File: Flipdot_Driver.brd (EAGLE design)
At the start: 160 x 100 mm, 27 parts

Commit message: Finished driver board design
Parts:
- added U$6: 3_PIN, Flipdot:3_PIN
- moved U$5 197.9 mm to (114.9, 74.2)
- moved U$4 155.3 mm to (126.9, 26.2)
- moved U$11 125.5 mm to (-22.1, 78.2), turned to 270 degrees
- moved U$10 116.5 mm to (-10.1, 76.2), turned to 270 degrees
- moved U$3 52.2 mm to (-24.0, 37.2), turned to 270 degrees
- moved SUBSEG 19.1 mm to (-16.5, 30.8)
- moved U$2 11.5 mm to (-20.7, -0.60), turned to 90 degrees
- moved COL_D_HL 0.58 mm to (88.3, 78.0)
- moved ROW_L 0.22 mm to (113.0, 53.7)
- moved SINK_R 0.22 mm to (101.9, 48.5)
- moved SOURCE_D 0.22 mm to (84.4, 64.1)
- moved COL_C_H 0.22 mm to (16.8, 75.9)
- moved COL_C_L 0.22 mm to (39.8, 75.9)
- moved SINK_C 0.22 mm to (37.3, 64.8)
- moved U$1 0.22 mm to (60.4, 40.8)
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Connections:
- net A: now also U$6.P$1
- net B: now also U$6.P$2
- net C: now also U$6.P$3
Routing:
- net N$13: track 0.00 -> 334.1 mm, vias 0 -> 2
- net 5V: track 174.3 -> 456.0 mm, vias 2 -> 12
- net GND: track 458.8 -> 685.9 mm, vias 2 -> 6
- net 10V: track 114.8 -> 313.9 mm, vias 2 -> 9
- net N$7: track 0.00 -> 159.8 mm, vias 0 -> 4
- net N$9: track 0.00 -> 156.1 mm, vias 0 -> 2
- net N$12: track 0.00 -> 115.1 mm, vias 0 -> 2
- net N$10: track 0.00 -> 108.1 mm, vias 0 -> 2
- net N$11: track 0.00 -> 87.8 mm
- net N$8: track 0.00 -> 85.2 mm, vias 0 -> 4
- net SEG_1: track 0.00 -> 71.4 mm, vias 0 -> 1
- net B: track 195.4 -> 251.5 mm, vias 3 -> 9
- net A: track 181.7 -> 229.7 mm, vias 7 -> 10
- net C: track 196.2 -> 240.8 mm, vias 4 -> 5
- net N$80: track 0.00 -> 14.9 mm
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
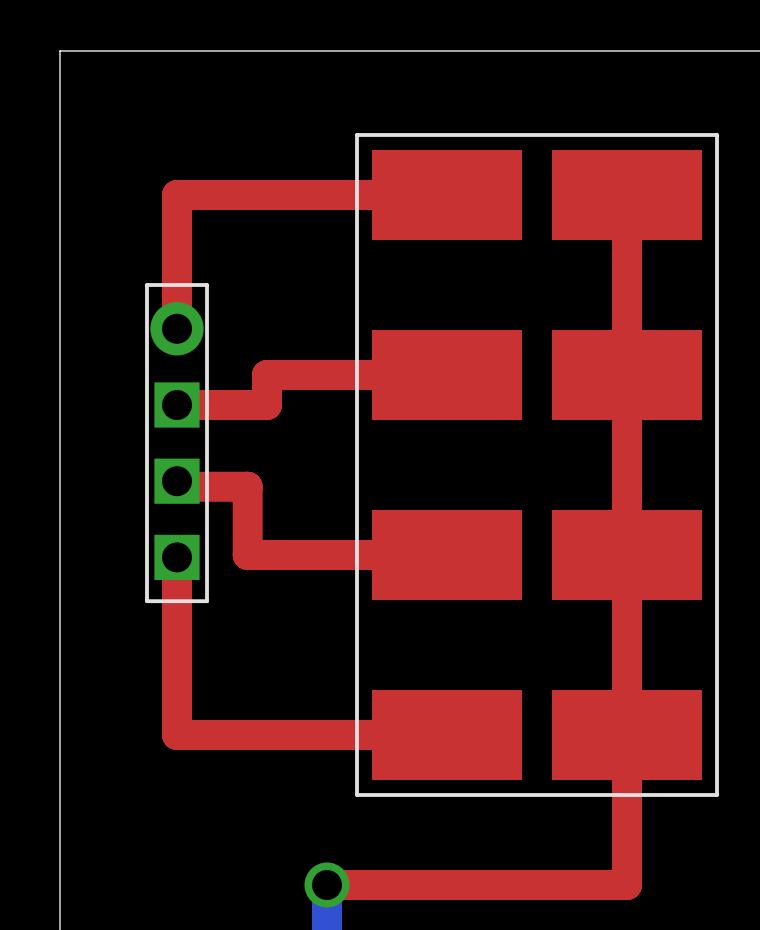
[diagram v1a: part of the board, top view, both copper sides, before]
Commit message: Fixed layering issue, finished printing stencil
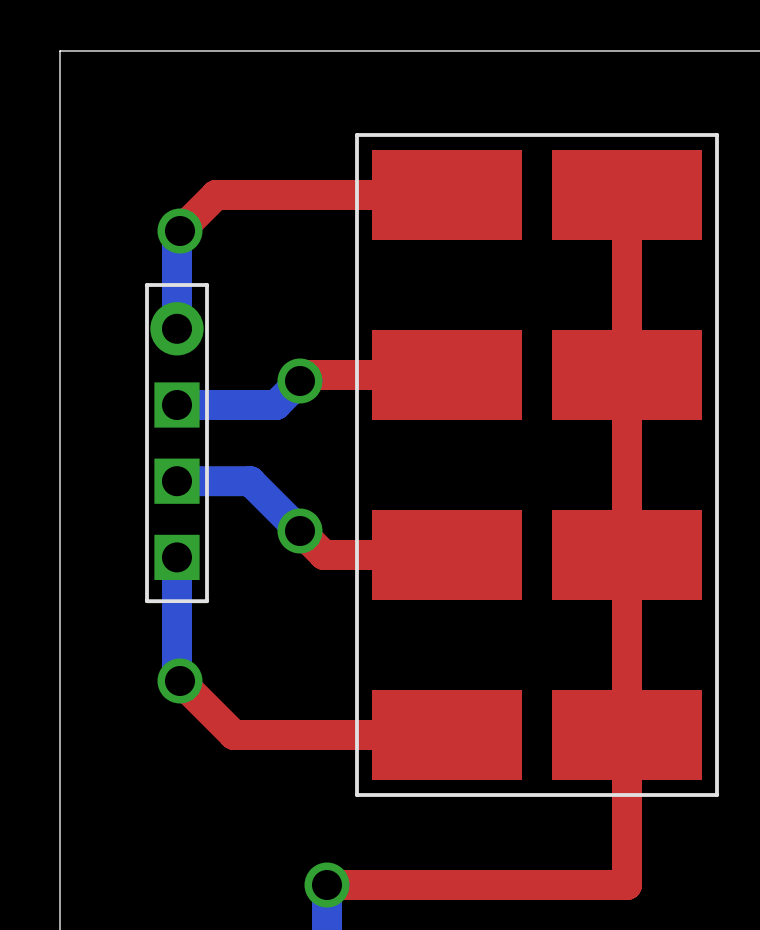
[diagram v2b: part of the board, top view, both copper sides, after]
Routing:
- net N$3: track 11.5 -> 10.0 mm, vias 0 -> 1
- net N$80: track 14.9 -> 13.8 mm, vias 0 -> 1
- net N$1: track 13.5 -> 12.7 mm, vias 0 -> 1
- net N$2: track 10.0 -> 9.41 mm, vias 0 -> 1
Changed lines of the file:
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@@
 <wire x1="134" y1="90" x2="-26" y2="90" width="0" layer="20"/>
 <wire x1="-26" y1="90" x2="-26" y2="-10" width="0" layer="20"/>
-<dimension x1="134" y1="-10" x2="134" y2="90" x3="138" y3="40" textsize="1.778" layer="20"/>
-<dimension x1="134" y1="90" x2="-26" y2="90" x3="54" y3="93" textsize="1.778" layer="20"/>
 </plain>
 <attributes>
@@
 <contactref element="U$11" pad="P$1"/>
 <contactref element="U$10" pad="S1"/>
-<wire x1="-22.1" y1="80.74" x2="-22.1" y2="85.2" width="1" layer="1"/>
-<wire x1="-22.1" y1="85.2" x2="-13.1" y2="85.2" width="1" layer="1"/>
+<wire x1="-13.1" y1="85.2" x2="-20.8" y2="85.2" width="1" layer="1"/>
+<wire x1="-20.8" y1="85.2" x2="-22" y2="84" width="1" layer="1"/>
+<via x="-22" y="84" extent="1-16" drill="1"/>
+<wire x1="-22" y1="84" x2="-22.1" y2="83.9" width="1" layer="16"/>
+<wire x1="-22.1" y1="83.9" x2="-22.1" y2="80.74" width="1" layer="16"/>
 </signal>
 <signal name="N$2">
 <contactref element="U$11" pad="P$2"/>
 <contactref element="U$10" pad="S2"/>
-<wire x1="-22.1" y1="78.2" x2="-19.1" y2="78.2" width="1" layer="1"/>
-<wire x1="-19.1" y1="78.2" x2="-19.1" y2="79.2" width="1" layer="1"/>
-<wire x1="-19.1" y1="79.2" x2="-13.1" y2="79.2" width="1" layer="1"/>
+<wire x1="-13.1" y1="79.2" x2="-17.8" y2="79.2" width="1" layer="1"/>
+<wire x1="-17.8" y1="79.2" x2="-18" y2="79" width="1" layer="1"/>
+<via x="-18" y="79" extent="1-16" drill="1"/>
+<wire x1="-18" y1="79" x2="-18.8" y2="78.2" width="1" layer="16"/>
+<wire x1="-18.8" y1="78.2" x2="-22.1" y2="78.2" width="1" layer="16"/>
 </signal>
 <signal name="N$3">
 <contactref element="U$11" pad="P$3"/>
 <contactref element="U$10" pad="S3"/>
-<wire x1="-22.1" y1="75.66" x2="-22.1" y2="75.4756" width="1" layer="1"/>
-<wire x1="-22.1" y1="75.4756" x2="-19.7444" y2="75.4756" width="1" layer="1"/>
-<wire x1="-19.7444" y1="75.4756" x2="-19.7444" y2="73.2" width="1" layer="1"/>
-<wire x1="-19.7444" y1="73.2" x2="-13.1" y2="73.2" width="1" layer="1"/>
+<wire x1="-13.1" y1="73.2" x2="-17.2" y2="73.2" width="1" layer="1"/>
+<wire x1="-17.2" y1="73.2" x2="-18" y2="74" width="1" layer="1"/>
+<via x="-18" y="74" extent="1-16" drill="1"/>
+<wire x1="-18" y1="74" x2="-19.66" y2="75.66" width="1" layer="16"/>
+<wire x1="-19.66" y1="75.66" x2="-22.1" y2="75.66" width="1" layer="16"/>
 </signal>
 <signal name="N$80">
 <contactref element="U$11" pad="P$4"/>
 <contactref element="U$10" pad="S4"/>
-<wire x1="-22.1" y1="73.12" x2="-22.1" y2="67.2" width="1" layer="1"/>
-<wire x1="-22.1" y1="67.2" x2="-13.1" y2="67.2" width="1" layer="1"/>
+<wire x1="-13.1" y1="67.2" x2="-20.2" y2="67.2" width="1" layer="1"/>
+<wire x1="-20.2" y1="67.2" x2="-22" y2="69" width="1" layer="1"/>
+<via x="-22" y="69" extent="1-16" drill="1"/>
+<wire x1="-22" y1="69" x2="-22.1" y2="69.1" width="1" layer="16"/>
+<wire x1="-22.1" y1="69.1" x2="-22.1" y2="73.12" width="1" layer="16"/>
 </signal>
 <signal name="N$4">

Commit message: Finished, sent for production review
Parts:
- removed U$6: 3_PIN, Flipdot:3_PIN
- moved U$2 38.0 mm to (15.5, 10.8)
- moved U$3 33.1 mm to (6.62, 49.7), turned to 0 degrees
- moved U$11 31.2 mm to (5.97, 64.6)
- moved U$10 27.8 mm to (14.7, 63.5)
- moved COL_C_L 26.1 mm to (63.3, 64.5)
- moved SINK_C 26.1 mm to (60.8, 53.3)
- moved SOURCE_C 26.1 mm to (36.5, 53.3)
- moved COL_C_H 26.1 mm to (40.3, 64.5)
- moved SOURCE_D 25.8 mm to (107.9, 53.5)
- moved SINK_D 25.8 mm to (83.7, 53.4)
- moved COL_A_L 25.1 mm to (77.9, 10.5)
- moved SINK_A 25.1 mm to (80.3, 21.9)
- moved SOURCE_A 25.1 mm to (105.2, 21.7)
- moved COL_A_H 25.1 mm to (101.3, 10.4)
- moved COL_B_H 23.6 mm to (31.1, 10.5)
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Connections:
- net A: no longer U$6.P$1
- net B: no longer U$6.P$2
- net C: no longer U$6.P$3
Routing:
- net N$13: track 334.1 -> 120.7 mm, vias 2 -> 1
- net GND: track 685.9 -> 519.3 mm, vias 6 -> 3
- net 5V: track 456.0 -> 305.1 mm, vias 12 -> 3
- net 10V: track 313.9 -> 229.4 mm, vias 9 -> 2
- net N$7: track 159.8 -> 97.6 mm, vias 4 -> 2
- net N$8: track 85.2 -> 48.0 mm, vias 4 -> 2
- net N$10: track 108.1 -> 72.0 mm
- net N$9: track 156.1 -> 122.1 mm, vias 2 -> 0
- net C1: track 61.2 -> 37.0 mm
- net N$12: track 115.1 -> 91.5 mm
- net SEG_1: track 71.4 -> 48.4 mm
- net N$11: track 87.8 -> 65.4 mm
- net C3: track 59.1 -> 36.7 mm, vias 2 -> 1
- net C2: track 63.1 -> 41.5 mm
- net C20: track 68.1 -> 46.9 mm
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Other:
- board size 160 x 100 mm -> 146 x 75.9 mm
- board text added: "GND 5V 10V"
- board text added: "MCU 2 3 4"
- board text added: "MCU 5 6 7"
- board text added: "MCU 8 9 10"
- board text added: "Seg. Sel."
- board text added: "The cake is a lie."

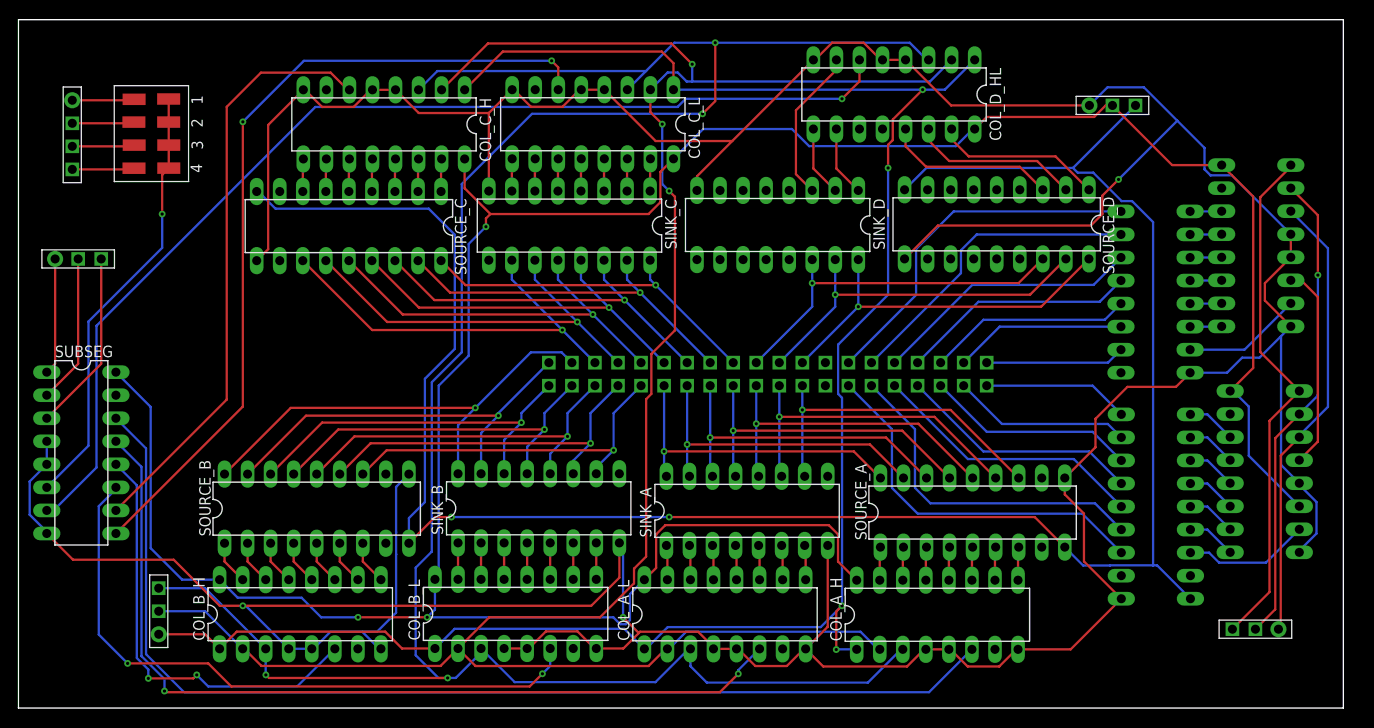
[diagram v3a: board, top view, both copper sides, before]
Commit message: Fixed missing RE connector
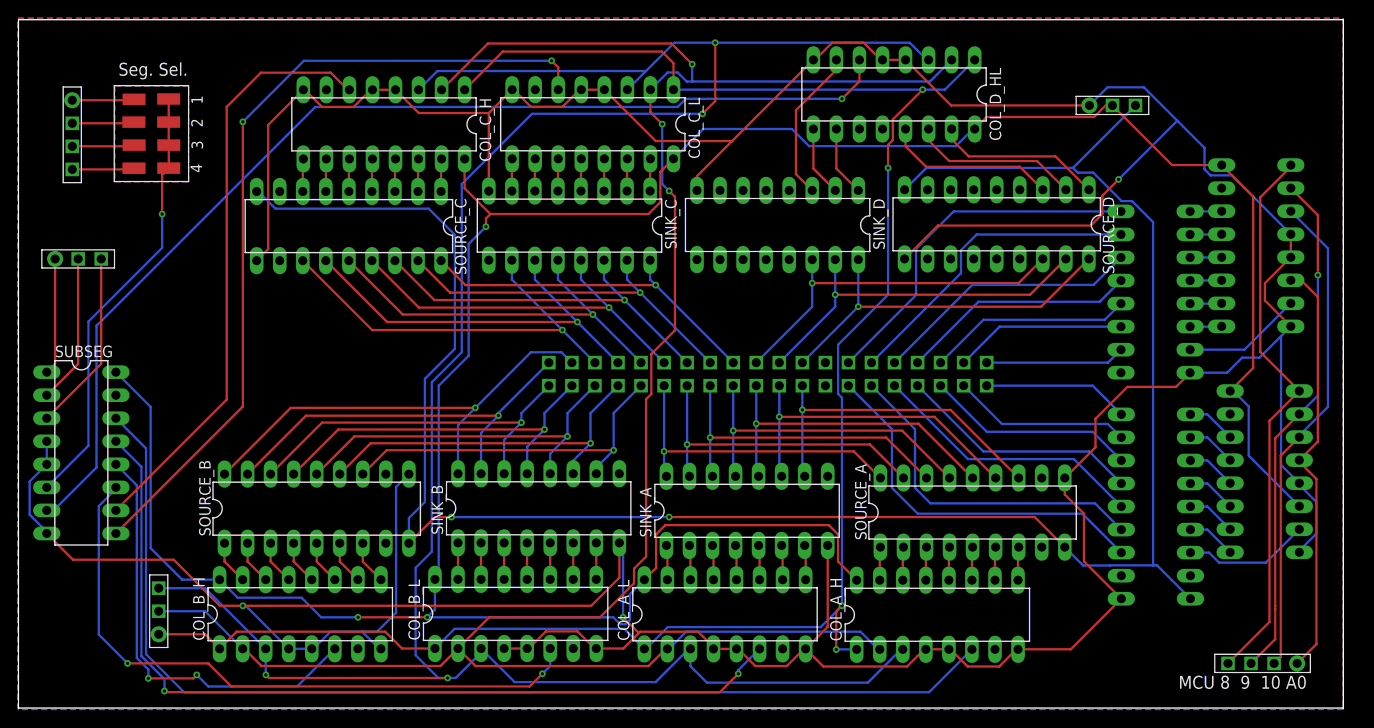
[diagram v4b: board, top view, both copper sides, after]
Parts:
- removed U$4: 3_PIN, Flipdot:3_PIN
- added U$6: 4_PIN, Flipdot:4_PIN
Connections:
- net N$62: now also U$6.P$4; no longer U$4.P$3
- net N$63: now also U$6.P$3; no longer U$4.P$2
- net N$64: now also U$6.P$2; no longer U$4.P$1
- net N$65: now also U$6.P$1
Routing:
- net N$65: track 22.6 -> 46.6 mm
- net N$63: track 52.7 -> 56.7 mm
- net N$62: track 57.4 -> 61.4 mm
- net N$64: track 50.1 -> 54.0 mm
- added copper zone on layer 1, net CUT
- added copper zone on layer 1, net GND
- added copper zone on layer 16, net GND
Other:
- board text added: "MCU 8 9 10 A0"
- board text removed: "MCU 8 9 10"
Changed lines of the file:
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@@
 <layer number="46" name="Milling" color="3" fill="1" visible="no" active="yes"/>
 <layer number="47" name="Measures" color="7" fill="1" visible="no" active="yes"/>
-<layer number="48" name="Document" color="7" fill="1" visible="no" active="yes"/>
+<layer number="48" name="Document" color="7" fill="1" visible="yes" active="yes"/>
 <layer number="49" name="Reference" color="7" fill="1" visible="no" active="yes"/>
 <layer number="50" name="dxf" color="7" fill="1" visible="no" active="no"/>
@@
 <wire x1="146.065" y1="76.03" x2="0.035" y2="76.03" width="0" layer="20"/>
 <wire x1="0.035" y1="76.03" x2="0.035" y2="0.16" width="0" layer="20"/>
-<text x="127.635" y="6.096" size="1.4224" layer="51">MCU  8  9  10</text>
 <text x="113.665" y="68.58" size="1.4224" layer="51">GND  5V  10V</text>
 <text x="18.161" y="2.921" size="1.4224" layer="51" rot="R90">MCU 2  3  4</text>
 <text x="2.54" y="52.07" size="1.4224" layer="51">MCU 5  6  7</text>
 <text x="26.543" y="37.592" size="1.778" layer="51">The cake is a lie.</text>
-<text x="11.049" y="69.85" size="1.4224" layer="51">Seg. Sel.</text>
+<text x="127.889" y="2.286" size="1.4224" layer="25">MCU 8  9  10 A0</text>
+<text x="11.049" y="69.85" size="1.4224" layer="25">Seg. Sel.</text>
 </plain>
 <attributes>
@@
 <element name="U$2" library="Flipdot" package="3_PIN" value="3_PIN" x="15.495" y="10.83" smashed="yes" rot="R90"/>
 <element name="U$3" library="Flipdot" package="3_PIN" value="3_PIN" x="6.615" y="49.66" smashed="yes"/>
-<element name="U$4" library="Flipdot" package="3_PIN" value="3_PIN" x="136.371" y="8.852" smashed="yes" rot="R180"/>
 <element name="U$10" library="Flipdot" package="JUMPER" value="JUMPER" x="14.665" y="63.5" smashed="yes" rot="R270"/>
 <element name="U$11" library="Flipdot" package="4_PIN" value="4_PIN" x="5.967" y="64.611" smashed="yes" rot="R270"/>
 <element name="U$5" library="Flipdot" package="3_PIN" value="3_PIN" x="120.615" y="66.58" smashed="yes"/>
+<element name="U$6" library="Flipdot" package="4_PIN" value="4_PIN" x="138.43" y="5.08" smashed="yes" rot="R180"/>
 </elements>
 <signals>
@@
 <wire x1="3.155" y1="19.5808625" x2="3.155" y2="19.4" width="0.254" layer="16"/>
 <wire x1="1.266" y1="21.4698625" x2="3.155" y2="19.5808625" width="0.254" layer="16"/>
+<polygon width="0.254" layer="1">
+<vertex x="0" y="76.2"/>
+<vertex x="146.05" y="76.2"/>
+<vertex x="146.05" y="0"/>
+<vertex x="0" y="0"/>
+</polygon>
+<polygon width="0.254" layer="16">
+<vertex x="0" y="0"/>
+<vertex x="0" y="76.2"/>
+<vertex x="146.05" y="76.2"/>
+<vertex x="146.05" y="0"/>
+</polygon>
 </signal>
 <signal name="5V">
@@
 <contactref element="ROW_L" pad="1"/>
 <contactref element="ROW_H" pad="1"/>
-<contactref element="U$4" pad="P$3"/>
-<wire x1="133.831" y1="8.852" x2="137.922" y2="12.943" width="0.254" layer="1"/>
 <wire x1="137.922" y1="31.815" x2="141.209" y2="35.102" width="0.254" layer="1"/>
-<wire x1="137.922" y1="12.943" x2="137.922" y2="31.815" width="0.254" layer="1"/>
 <wire x1="140.271" y1="59.8231375" x2="140.271" y2="60.004" width="0.254" layer="1"/>
 <wire x1="136.906" y1="39.405" x2="136.906" y2="56.4581375" width="0.254" layer="1"/>
 <wire x1="136.906" y1="56.4581375" x2="140.271" y2="59.8231375" width="0.254" layer="1"/>
 <wire x1="141.209" y1="35.102" x2="136.906" y2="39.405" width="0.254" layer="1"/>
+<contactref element="U$6" pad="P$4"/>
+<wire x1="133.35" y1="5.08" x2="137.922" y2="9.652" width="0.254" layer="1"/>
+<wire x1="137.922" y1="9.652" x2="137.922" y2="31.815" width="0.254" layer="1"/>
 </signal>
 <signal name="N$63">
 <contactref element="ROW_L" pad="2"/>
 <contactref element="ROW_H" pad="2"/>
-<contactref element="U$4" pad="P$2"/>
-<wire x1="136.371" y1="8.852" x2="138.557" y2="11.038" width="0.254" layer="1"/>
 <wire x1="138.557" y1="29.91" x2="141.209" y2="32.562" width="0.254" layer="1"/>
-<wire x1="138.557" y1="11.038" x2="138.557" y2="29.91" width="0.254" layer="1"/>
+<wire x1="138.557" y1="11.038" x2="138.557" y2="11.43" width="0.254" layer="1"/>
+<wire x1="138.557" y1="11.43" x2="138.557" y2="29.91" width="0.254" layer="1"/>
 <wire x1="141.209" y1="32.562" x2="143.256" y2="34.609" width="0.254" layer="16"/>
 <wire x1="143.256" y1="34.609" x2="143.256" y2="47.879" width="0.254" layer="16"/>
@@
 <wire x1="143.256" y1="47.879" x2="143.256" y2="54.479" width="0.254" layer="1"/>
 <wire x1="143.256" y1="54.479" x2="140.271" y2="57.464" width="0.254" layer="1"/>
+<contactref element="U$6" pad="P$3"/>
+<wire x1="135.89" y1="5.08" x2="138.557" y2="7.747" width="0.254" layer="1"/>
+<wire x1="138.557" y1="7.747" x2="138.557" y2="11.038" width="0.254" layer="1"/>
 </signal>
 <signal name="N$64">
 <contactref element="ROW_L" pad="3"/>
 <contactref element="ROW_H" pad="3"/>
-<contactref element="U$4" pad="P$1"/>
 <wire x1="141.232" y1="29.999" x2="141.209" y2="30.022" width="0.254" layer="16"/>
-<wire x1="139.165" y1="27.978" x2="139.165" y2="9.106" width="0.254" layer="1"/>
-<wire x1="138.911" y1="8.852" x2="139.165" y2="9.106" width="0.254" layer="1"/>
 <wire x1="139.165" y1="27.978" x2="141.209" y2="30.022" width="0.254" layer="1"/>
 <wire x1="141.232" y1="30.2258625" x2="141.232" y2="29.999" width="0.254" layer="16"/>
@@
 <wire x1="144.368" y1="50.827" x2="144.368" y2="33.3618625" width="0.254" layer="16"/>
 <wire x1="140.271" y1="54.924" x2="144.368" y2="50.827" width="0.254" layer="16"/>
+<contactref element="U$6" pad="P$2"/>
+<wire x1="138.43" y1="5.08" x2="139.165" y2="5.815" width="0.254" layer="1"/>
+<wire x1="139.165" y1="5.815" x2="139.165" y2="27.978" width="0.254" layer="1"/>
 </signal>
 <signal name="N$65">
@@
 <wire x1="143.256" y1="45.466" x2="141.418" y2="47.304" width="0.254" layer="1"/>
 <wire x1="141.418" y1="47.304" x2="140.271" y2="47.304" width="0.254" layer="1"/>
+<contactref element="U$6" pad="P$1"/>
+<wire x1="141.209" y1="27.482" x2="141.209" y2="27.3011375" width="0.254" layer="1"/>
+<wire x1="141.209" y1="27.3011375" x2="143.098" y2="25.4121375" width="0.254" layer="1"/>
+<wire x1="143.098" y1="25.4121375" x2="143.098" y2="7.208" width="0.254" layer="1"/>
+<wire x1="143.098" y1="7.208" x2="140.97" y2="5.08" width="0.254" layer="1"/>
 </signal>
 <signal name="N$66">
@@
 <wire x1="9.155" y1="38.1" x2="9.155" y2="49.66" width="0.254" layer="1"/>
 </signal>
+<signal name="CUT">
+<polygon width="0.254" layer="1" pour="cutout">
+<vertex x="10.668" y="58.166"/>
+<vertex x="18.796" y="58.166"/>
+<vertex x="18.796" y="68.58"/>
+<vertex x="18.796" y="68.707"/>
+<vertex x="10.668" y="68.707"/>
+<vertex x="10.668" y="58.293"/>
+</polygon>
+</signal>
 </signals>
